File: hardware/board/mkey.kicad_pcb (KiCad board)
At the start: 2 copper layers, 346.2 x 95.5 mm, 171 parts, among them J1 USB_C_REP_2.0, J2 24 pin LCD FPC connector, SW0 SW_Push, SW1 SW_Push, U1 ESP32-S3-WROOM-1, U2 SY8088

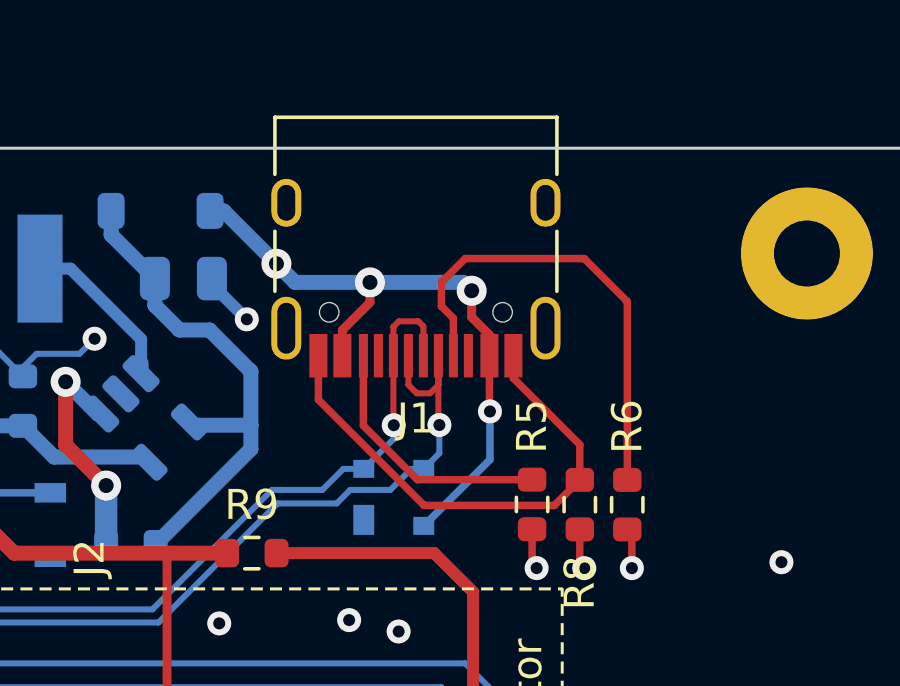
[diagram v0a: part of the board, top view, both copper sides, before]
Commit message: fix that the USB pins were swapped
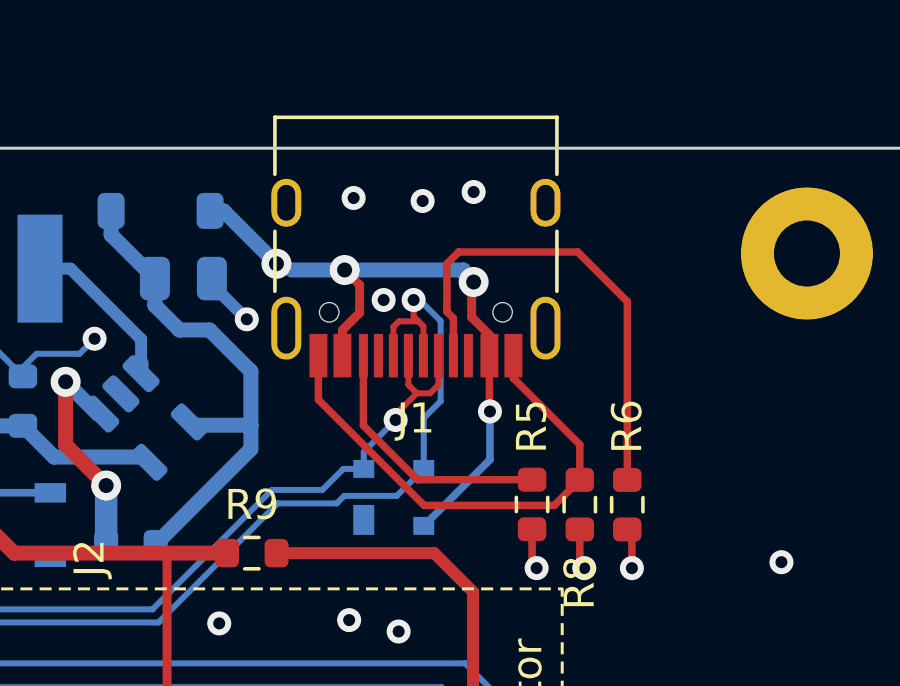
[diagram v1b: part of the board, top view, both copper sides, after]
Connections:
- J1 pad A6: USB_D- -> USB_D+
- J1 pad A7: USB_D+ -> USB_D-
- J1 pad B6: USB_D- -> USB_D+
- J1 pad B7: USB_D+ -> USB_D-
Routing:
- net USB_D+: track 41.0 -> 43.9 mm
- net USB_D-: track 38.5 -> 37.7 mm
- net GND: vias 149 -> 153
